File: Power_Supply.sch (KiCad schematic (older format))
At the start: 1 part

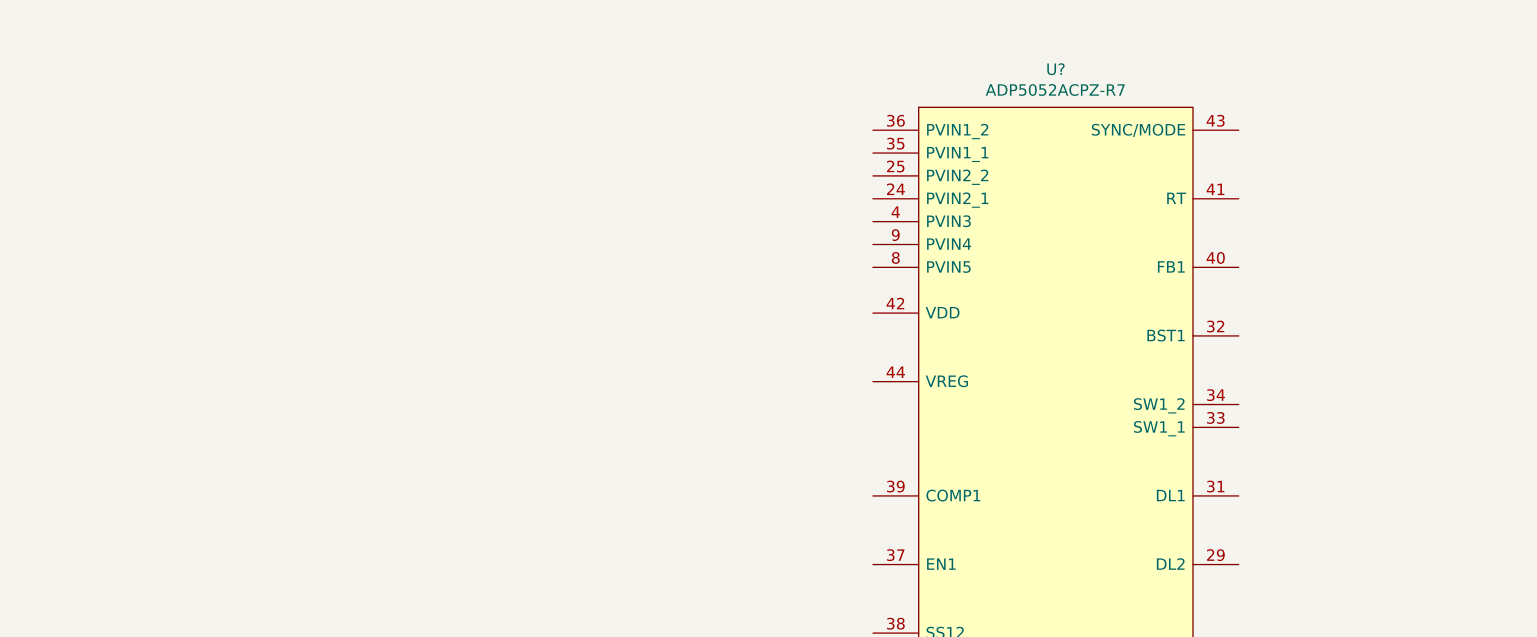
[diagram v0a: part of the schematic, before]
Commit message: Power_Supply Sch partially completed
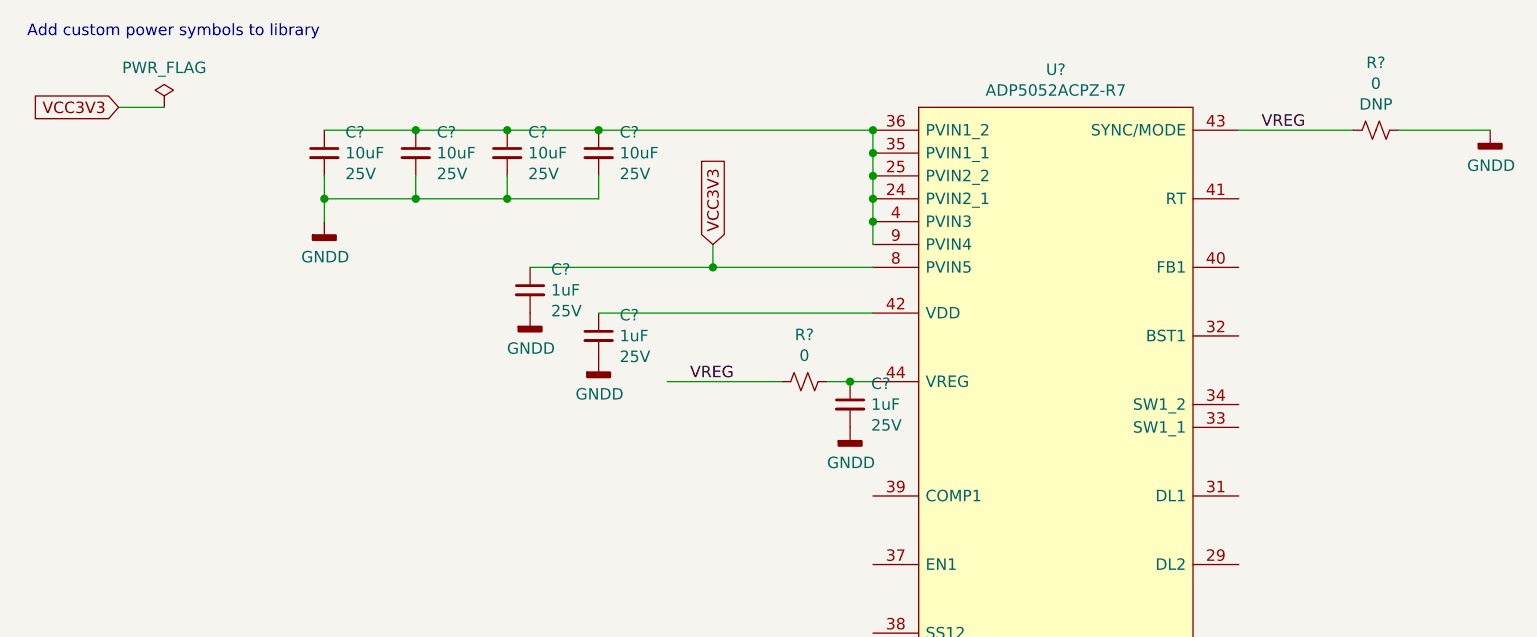
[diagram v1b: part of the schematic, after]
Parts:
- added C? (x4): 10uF, Capacitor_SMD:C_0805_2012Metric_Pad1.18x1.45mm_HandSolder, symbol Device:C_Small
- added C? (x3): 1uF, Capacitor_SMD:C_0201_0603Metric_Pad0.64x0.40mm_HandSolder, symbol Device:C_Small
- added R? (x2): 0, Resistor_SMD:R_0603_1608Metric_Pad0.98x0.95mm_HandSolder, symbol Device:R_Small_US
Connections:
- net labels added: GNDD, VCC3V3, VREG
- wire segments 0 -> 27
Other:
- note added: "Add custom power symbols to library"

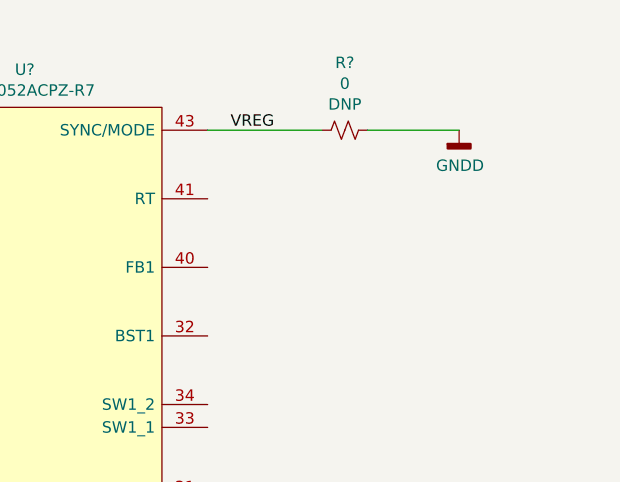
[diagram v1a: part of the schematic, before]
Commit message: Added parts to the FPGA_Power
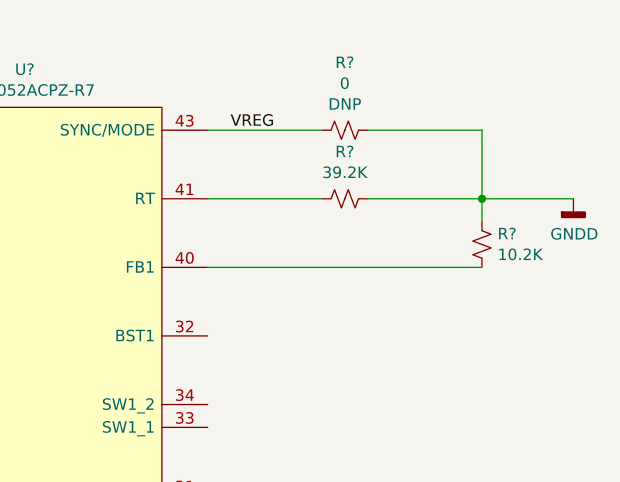
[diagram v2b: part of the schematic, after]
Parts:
- added R?: 39.2K, Resistor_SMD:R_0603_1608Metric_Pad0.98x0.95mm_HandSolder, symbol Device:R_Small_US
- added R?: 10.2K, Resistor_SMD:R_0603_1608Metric_Pad0.98x0.95mm_HandSolder, symbol Device:R_Small_US
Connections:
- wire segments 27 -> 33
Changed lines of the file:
@@
 L power:GNDD #PWR?
 U 1 1 601FA970
-P 7000 1000
-F 0 "#PWR?" H 7000 750 50  0001 C CNN
-F 1 "GNDD" H 7004 845 50  0000 C CNN
-F 2 "" H 7000 1000 50  0001 C CNN
-F 3 "" H 7000 1000 50  0001 C CNN
-	1    7000 1000
+P 7500 1300
+F 0 "#PWR?" H 7500 1050 50  0001 C CNN
+F 1 "GNDD" H 7504 1145 50  0000 C CNN
+F 2 "" H 7500 1300 50  0001 C CNN
+F 3 "" H 7500 1300 50  0001 C CNN
+	1    7500 1300
 	1    0    0    -1
 $EndComp
@@
 	5900 1000 6400 1000
 Wire Wire Line
-	6600 1000 7000 1000
+	7100 1300 7500 1300
 Text Label 6000 1000 0    50   ~ 0
 VREG
+$Comp
+L Device:R_Small_US R?
+U 1 1 601DB89B
+P 6500 1300
+F 0 "R?" V 6295 1300 50  0000 C CNN
+F 1 "39.2K" V 6386 1300 50  0000 C CNN
+F 2 "Resistor_SMD:R_0603_1608Metric_Pad0.98x0.95mm_HandSolder" H 6500 1300 50  0001 C CNN
+F 3 "~" H 6500 1300 50  0001 C CNN
+F 4 "" V 6500 1300 50  0001 C CNN "MPN"
+	1    6500 1300
+	0    1    1    0
+$EndComp
+Wire Wire Line
+	6400 1300 5900 1300
+Wire Wire Line
+	6600 1000 7100 1000
+Wire Wire Line
+	7100 1000 7100 1300
+Wire Wire Line
+	6600 1300 7100 1300
+Connection ~ 7100 1300
+$Comp
+L Device:R_Small_US R?
+U 1 1 601E0C1C
+P 7100 1500
+F 0 "R?" H 7032 1454 50  0000 R CNN
+F 1 "10.2K" H 7032 1545 50  0000 R CNN
+F 2 "Resistor_SMD:R_0603_1608Metric_Pad0.98x0.95mm_HandSolder" H 7100 1500 50  0001 C CNN
+F 3 "~" H 7100 1500 50  0001 C CNN
+	1    7100 1500
+	-1   0    0    1
+$EndComp
+Wire Wire Line
+	7100 1400 7100 1300
+Wire Wire Line
+	5900 1600 7100 1600
 $EndSCHEMATC

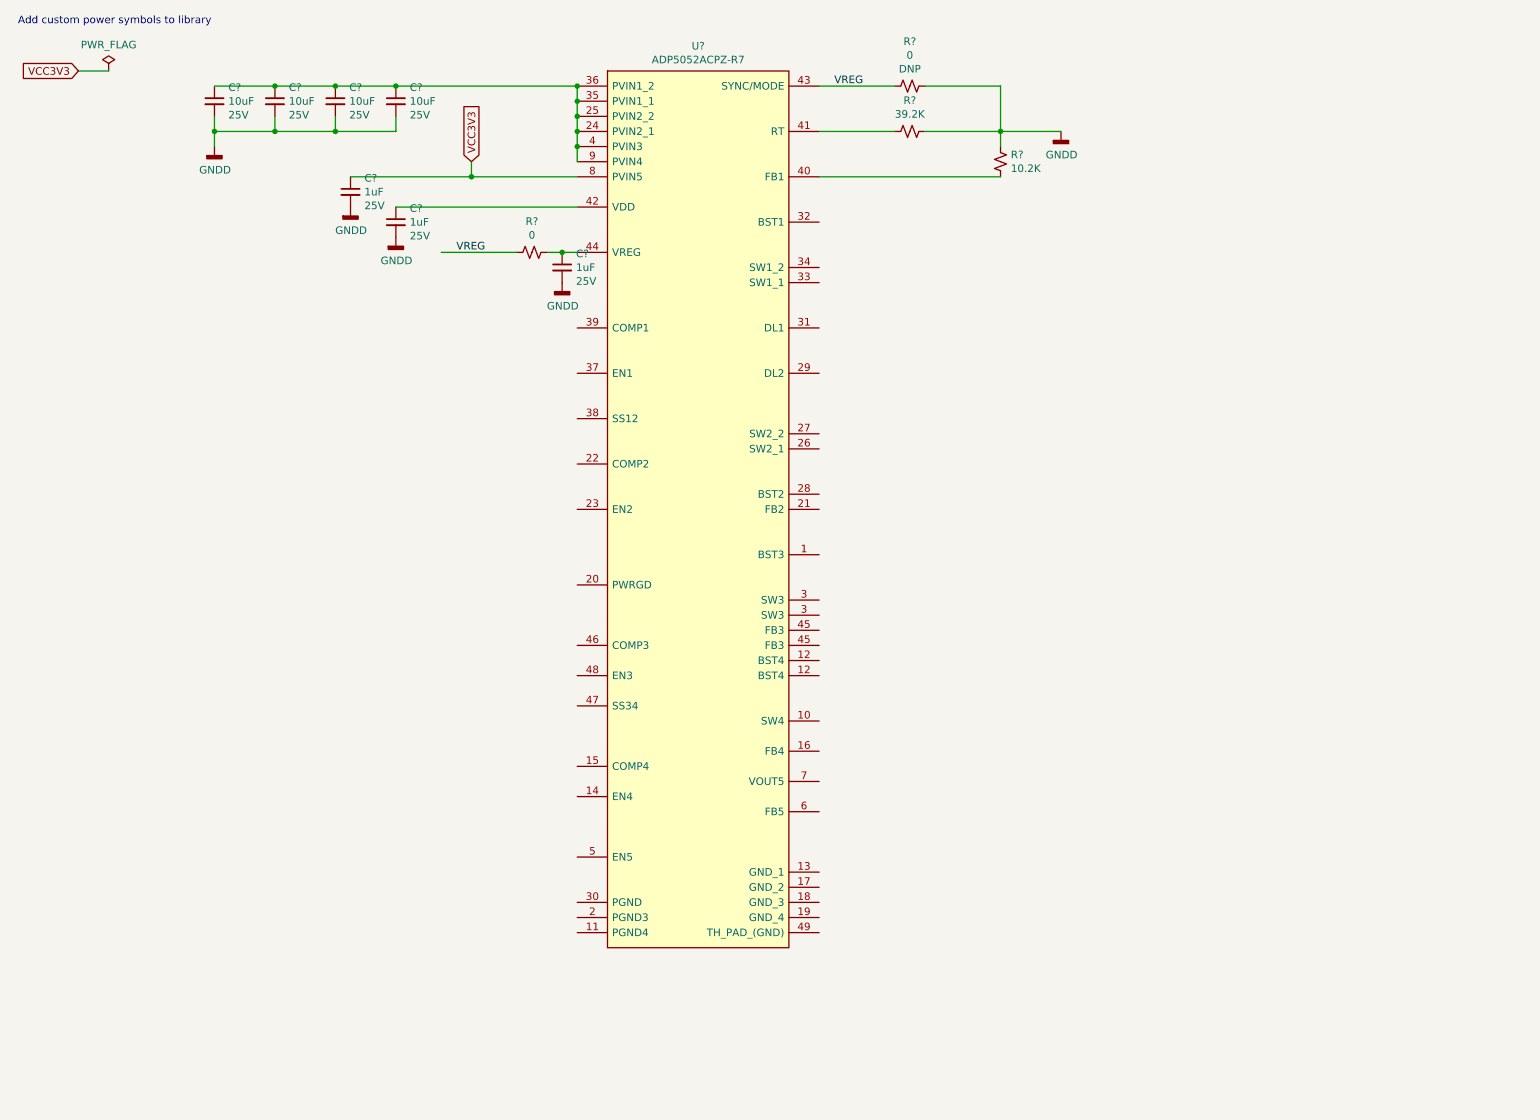
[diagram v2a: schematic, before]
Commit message: Completeed the FPGA_Power sheet Created PCB
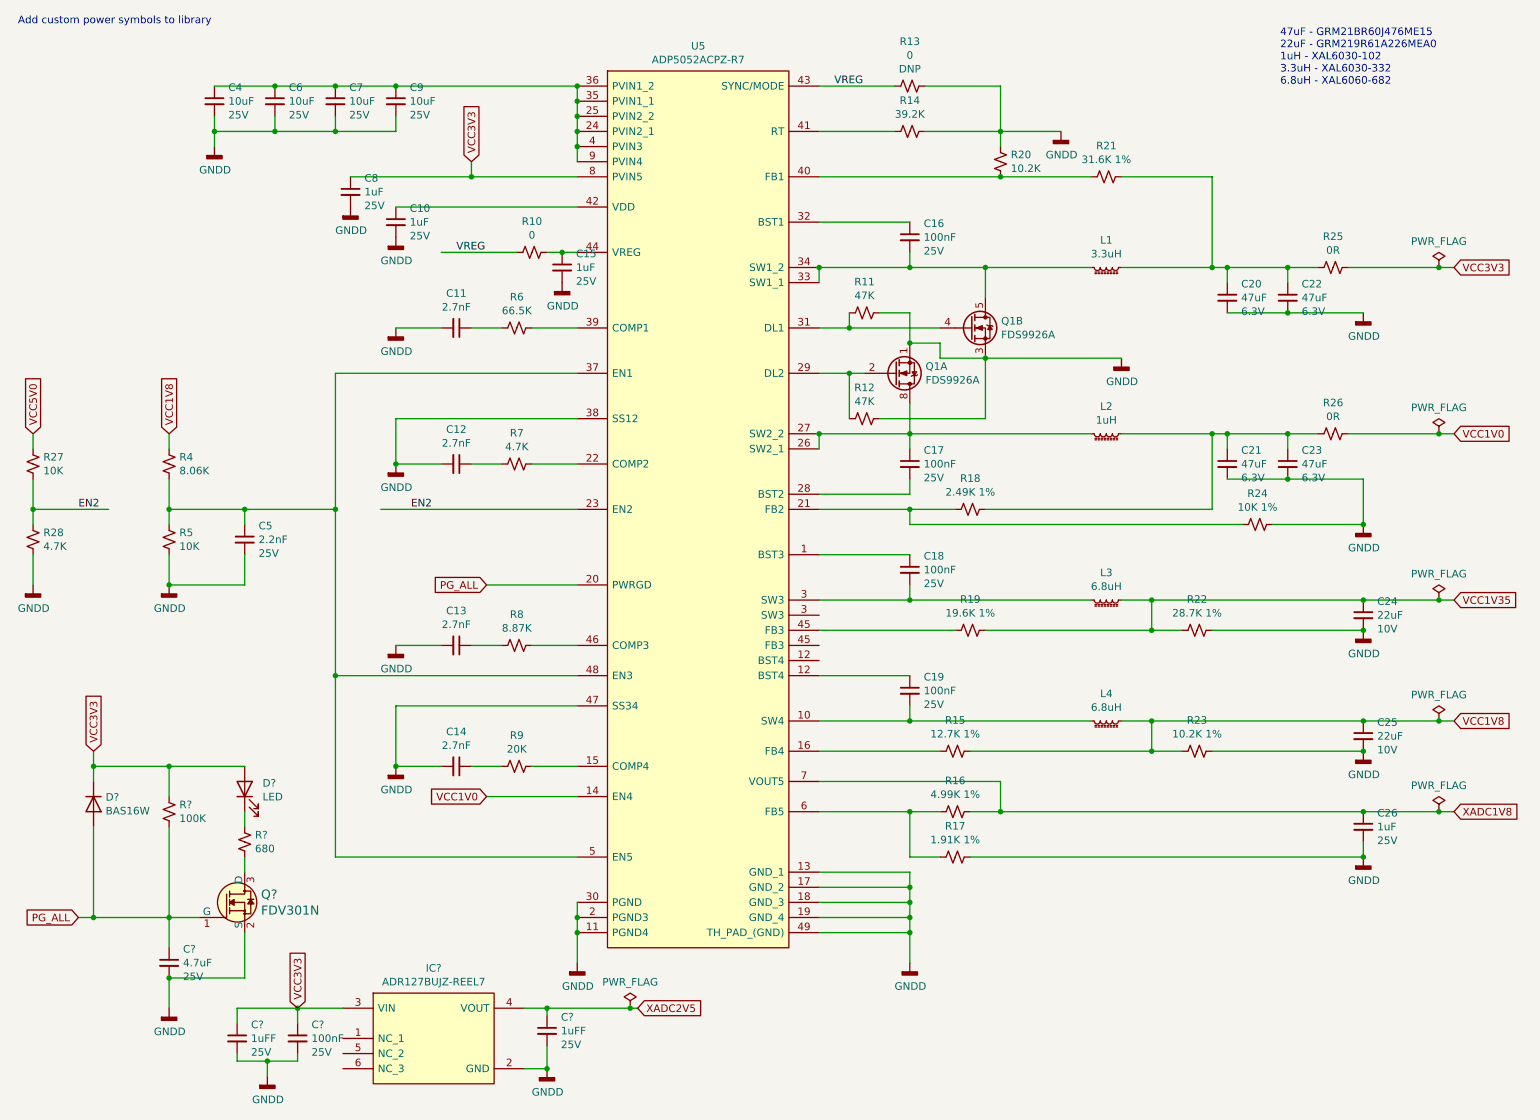
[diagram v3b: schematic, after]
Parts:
- added C11, C12, C13, C14: 2.7nF, Capacitor_SMD:C_0603_1608Metric_Pad1.08x0.95mm_HandSolder, symbol Device:C_Small
- added C16, C17, C18, C19, C?: 100nF, Capacitor_SMD:C_0603_1608Metric_Pad1.08x0.95mm_HandSolder, symbol Device:C_Small
- added C20, C21, C22, C23: 47uF, Capacitor_SMD:C_0805_2012Metric_Pad1.18x1.45mm_HandSolder, symbol Device:C_Small
- added C24, C25: 22uF, Capacitor_SMD:C_0805_2012Metric_Pad1.18x1.45mm_HandSolder, symbol Device:C_Small
- added C26: 1uF, Capacitor_SMD:C_0603_1608Metric_Pad1.08x0.95mm_HandSolder, symbol Device:C_Small
- added C5: 2.2nF, Capacitor_SMD:C_0603_1608Metric_Pad1.08x0.95mm_HandSolder, symbol Device:C_Small
- added C?: 4.7uF, Capacitor_SMD:C_0603_1608Metric_Pad1.08x0.95mm_HandSolder, symbol Device:C_Small
- added C? (x2): 1uFF, Capacitor_SMD:C_0603_1608Metric_Pad1.08x0.95mm_HandSolder, symbol Device:C_Small
- added D?: BAS16W, Package_TO_SOT_SMD:SOT-323_SC-70, symbol Diode:BAS16W
- added D?: LED, LED_SMD:LED_0603_1608Metric_Pad1.05x0.95mm_HandSolder, symbol Device:LED
- added IC?: ADR127BUJZ-REEL7, SOT95P280X100-6N, symbol GM_Voltage_Regulators:ADR127BUJZ-REEL7
- added L1: 3.3uH, symbol Device:L_Ferrite_Small
- added L2: 1uH, symbol Device:L_Ferrite_Small
- added L3, L4: 6.8uH, symbol Device:L_Ferrite_Small
- added Q1: FDS9926A, Package_SO:SOIC-8_3.9x4.9mm_P1.27mm, symbol Transistor_FET:FDS9926A
- added Q?: FDV301N, digikey-footprints:SOT-23-3, symbol dk_Transistors-FETs-MOSFETs-Single:FDV301N
- added R11, R12: 47K, Resistor_SMD:R_0603_1608Metric_Pad0.98x0.95mm_HandSolder, symbol Device:R_Small_US
- added R15: 12.7K 1%, Resistor_SMD:R_0603_1608Metric_Pad0.98x0.95mm_HandSolder, symbol Device:R_Small_US
- added R16: 4.99K 1%, Resistor_SMD:R_0603_1608Metric_Pad0.98x0.95mm_HandSolder, symbol Device:R_Small_US
- added R17: 1.91K 1%, Resistor_SMD:R_0603_1608Metric_Pad0.98x0.95mm_HandSolder, symbol Device:R_Small_US
- added R18: 2.49K 1%, Resistor_SMD:R_0603_1608Metric_Pad0.98x0.95mm_HandSolder, symbol Device:R_Small_US
- added R19: 19.6K 1%, Resistor_SMD:R_0603_1608Metric_Pad0.98x0.95mm_HandSolder, symbol Device:R_Small_US
- added R21: 31.6K 1%, Resistor_SMD:R_0603_1608Metric_Pad0.98x0.95mm_HandSolder, symbol Device:R_Small_US
- added R22: 28.7K 1%, Resistor_SMD:R_0603_1608Metric_Pad0.98x0.95mm_HandSolder, symbol Device:R_Small_US
- added R23: 10.2K 1%, Resistor_SMD:R_0603_1608Metric_Pad0.98x0.95mm_HandSolder, symbol Device:R_Small_US
- added R24: 10K 1%, Resistor_SMD:R_0603_1608Metric_Pad0.98x0.95mm_HandSolder, symbol Device:R_Small_US
- added R25, R26: 0R, Resistor_SMD:R_0805_2012Metric_Pad1.20x1.40mm_HandSolder, symbol Device:R_Small_US
- added R27, R5: 10K, Resistor_SMD:R_0603_1608Metric_Pad0.98x0.95mm_HandSolder, symbol Device:R_Small_US
- added R28, R7: 4.7K, Resistor_SMD:R_0603_1608Metric_Pad0.98x0.95mm_HandSolder, symbol Device:R_Small_US
- added R4: 8.06K, Resistor_SMD:R_0603_1608Metric_Pad0.98x0.95mm_HandSolder, symbol Device:R_Small_US
- added R6: 66.5K, Resistor_SMD:R_0603_1608Metric_Pad0.98x0.95mm_HandSolder, symbol Device:R_Small_US
- added R8: 8.87K, Resistor_SMD:R_0603_1608Metric_Pad0.98x0.95mm_HandSolder, symbol Device:R_Small_US
- added R9: 20K, Resistor_SMD:R_0603_1608Metric_Pad0.98x0.95mm_HandSolder, symbol Device:R_Small_US
- added R?: 100K, Resistor_SMD:R_0603_1608Metric_Pad0.98x0.95mm_HandSolder, symbol Device:R_Small_US
- added R?: 680, Resistor_SMD:R_0603_1608Metric_Pad0.98x0.95mm_HandSolder, symbol Device:R_Small_US
- C10, C15, C8: renamed from C?; footprint Capacitor_SMD:C_0201_0603Metric_Pad0.64x0.40mm_HandSolder -> Capacitor_SMD:C_0603_1608Metric_Pad1.08x0.95mm_HandSolder; MPN TMK107BLD105MA-T -> (none)
- C4, C6, C7, C9: renamed from C?; MPN TMK212BC6106KG-T -> (none)
- gave numbers to parts that had none: 5
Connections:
- net labels added: EN2, PG_ALL, VCC1V0, VCC1V35, VCC1V8, VCC5V0, XADC1V8, XADC2V5
- wire segments 33 -> 212
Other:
- note added: "47uF - GRM21BR60J476ME15\n22uF - GRM219R61A226MEA0\n1uH - XAL6030-102\n3.3uH - XAL6030-332\n6.8uH - XAL6060-682"

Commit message: Added power symbol to EEPROM sheet
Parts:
- U5: symbol GM_Voltage_Regulators:ADP5052ACPZ-R7 -> Digital_Board-rescue:ADP5052ACPZ-R7-GM_Voltage_Regulators
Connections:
- net at U5.12 (BST4): now also C19.1
- net at U5.3 (SW3): now also C18.2, L3.2
- net at U5.45 (FB3): now also R19.2
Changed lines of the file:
@@
 $EndDescr
 $Comp
-L GM_Voltage_Regulators:ADP5052ACPZ-R7 U5
+L Digital_Board-rescue:ADP5052ACPZ-R7-GM_Voltage_Regulators U5
 U 1 1 601DF1D0
 P 4500 900
+AR Path="/601DF1D0" Ref="U5"  Part="1"
+AR Path="/601DF0A6/601DF1D0" Ref="U5"  Part="1"
 F 0 "U5" H 5100 1065 50  0000 C CNN
 F 1 "ADP5052ACPZ-R7" H 5100 974 50  0000 C CNN
